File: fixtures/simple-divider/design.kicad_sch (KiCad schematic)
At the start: 2 parts

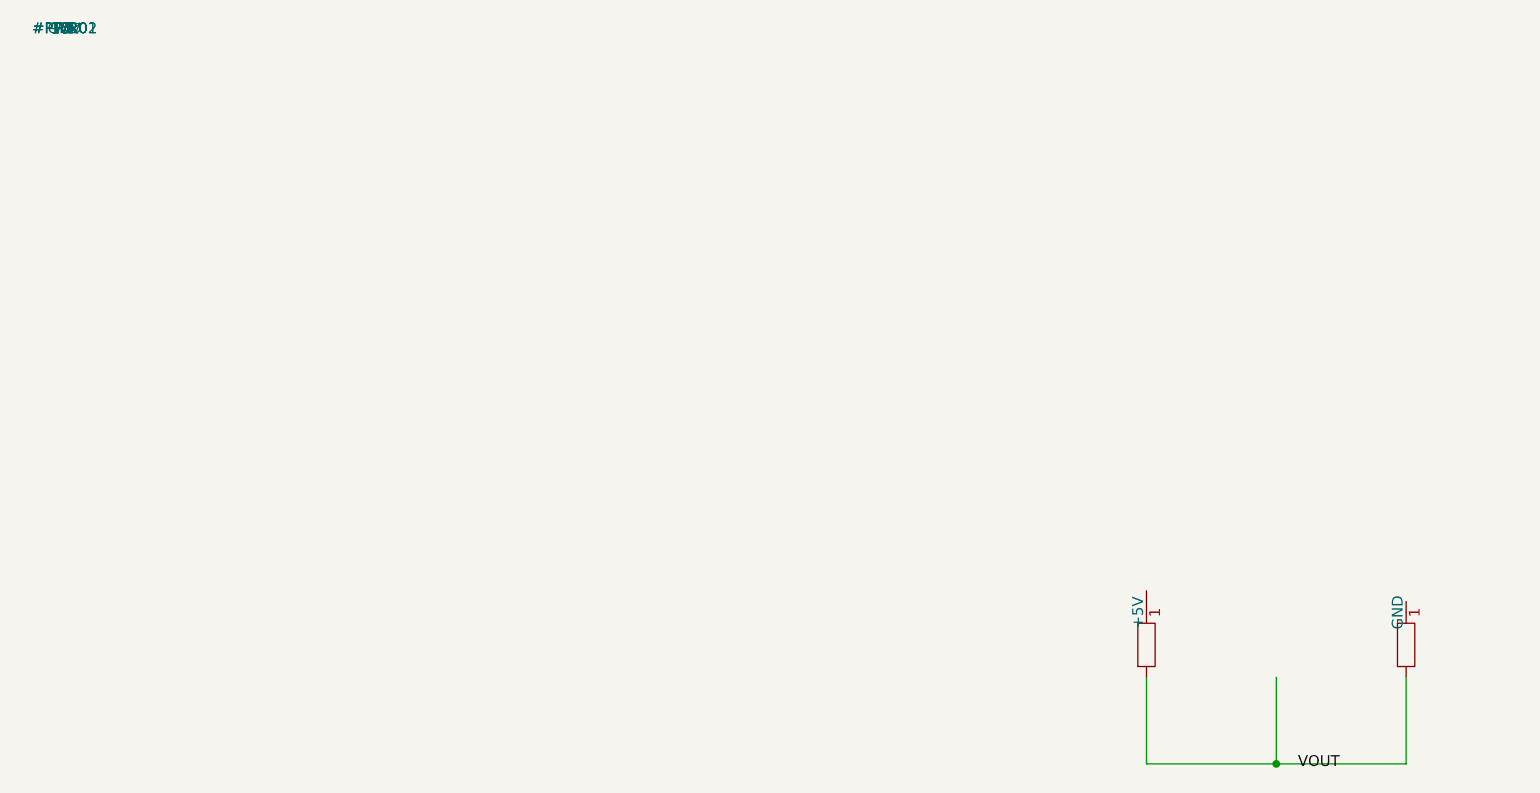
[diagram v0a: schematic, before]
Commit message: fix: фикстуры под реальный контейнер — PWR_FLAG, checks.spice инжект, ngspice без -r, путь анализатора
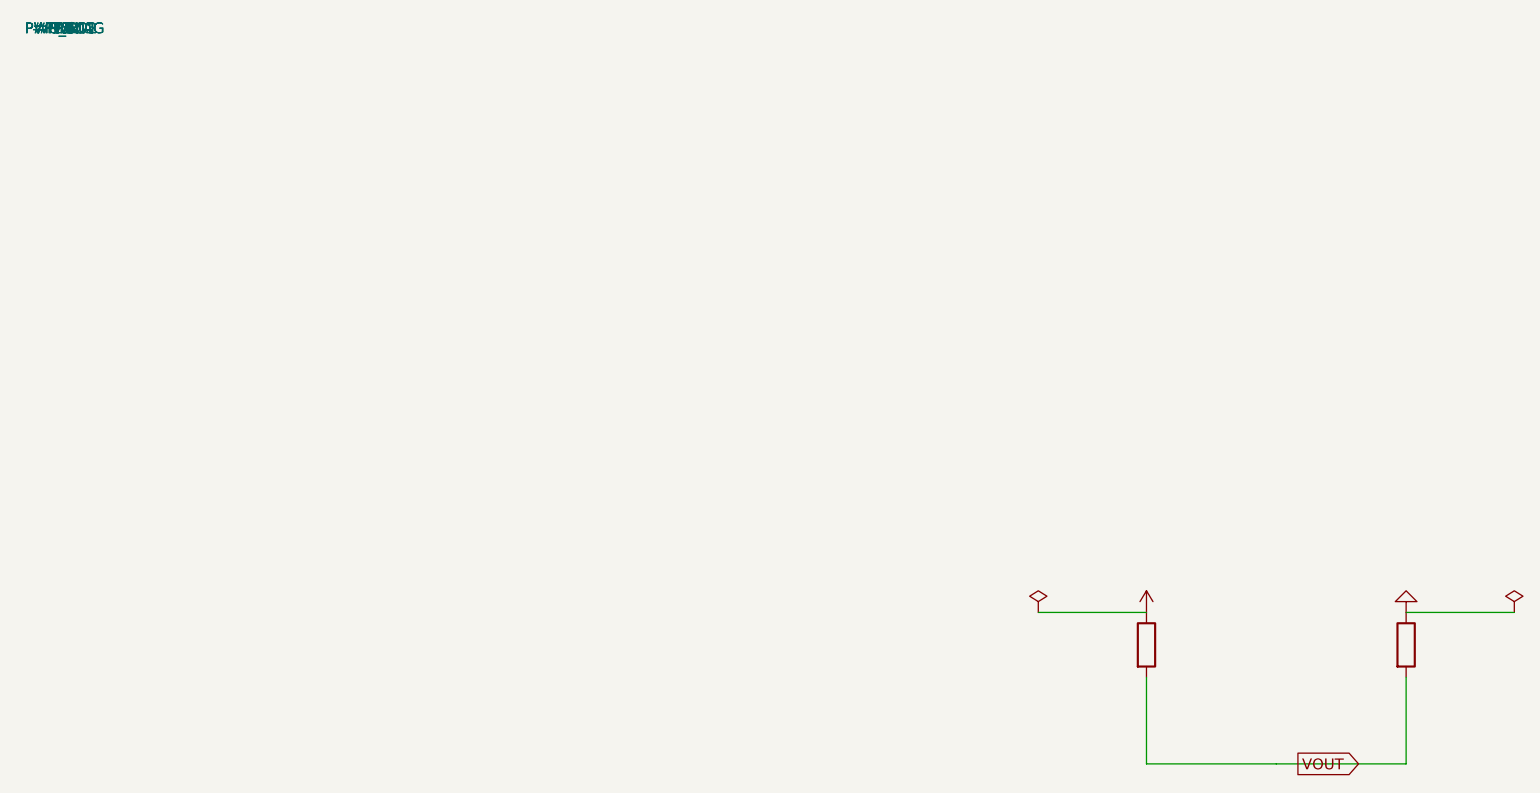
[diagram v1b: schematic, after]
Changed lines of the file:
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@@
     (title "simple-divider")
   )
-  (junction (at 142.24 86.36) (diameter 0) (color 0 0 0 0))
+  (wire (pts (xy 114.3 68.58) (xy 127 68.58)) (stroke (width 0) (type default)))
   (wire (pts (xy 127 76.2) (xy 127 86.36)) (stroke (width 0) (type default)))
   (wire (pts (xy 127 86.36) (xy 142.24 86.36)) (stroke (width 0) (type default)))
-  (wire (pts (xy 142.24 76.2) (xy 142.24 86.36)) (stroke (width 0) (type default)))
   (wire (pts (xy 142.24 86.36) (xy 157.48 86.36)) (stroke (width 0) (type default)))
+  (wire (pts (xy 157.48 68.58) (xy 170.18 68.58)) (stroke (width 0) (type default)))
   (wire (pts (xy 157.48 76.2) (xy 157.48 86.36)) (stroke (width 0) (type default)))
   (symbol (lib_id "power:+5V") (at 127 68.58 0) (unit 1)
@@
     (pin "1")
   )
-  (label "VOUT" (at 144.78 86.36 0))
+  (symbol (lib_id "power:PWR_FLAG") (at 114.3 68.58 0) (unit 1)
+    (property "Reference" "#FLG01")
+    (property "Value" "PWR_FLAG")
+    (pin "1")
+  )
+  (symbol (lib_id "power:PWR_FLAG") (at 170.18 68.58 0) (unit 1)
+    (property "Reference" "#FLG02")
+    (property "Value" "PWR_FLAG")
+    (pin "1")
+  )
+  (global_label "VOUT" (shape output) (at 144.78 86.36 0)
+    (effects (font (size 1.27 1.27)) (justify left))
+  )
 )
